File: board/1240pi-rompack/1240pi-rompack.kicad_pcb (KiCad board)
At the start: 4 copper layers, 73.7 x 50.8 mm, 5 parts, among them J1 HDMI_A, J2 HDMI_A, P1 CardEdge_ROMPACK

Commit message: Add more stuff to rompack board.
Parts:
- added R1: 470R, Resistor_SMD:R_0603_1608Metric, F.Cu at (144.8, 81.3)
- added R2: 470R, Resistor_SMD:R_0603_1608Metric, F.Cu at (148.8, 81.3)
- added REF**: QFN-48-1EP_7x7mm_P0.5mm_EP5.15x5.15mm, Package_DFN_QFN:QFN-48-1EP_7x7mm_P0.5mm_EP5.15x5.15mm, F.Cu at (147.3, 94.0)
- added REF**: VQFP-100_14x14mm_P0.5mm, Package_QFP:VQFP-100_14x14mm_P0.5mm, F.Cu at (168.9, 83.8)
- moved J1 9.17 mm to (177.8, 104.9)
- moved J2 9.17 mm to (158.8, 104.9)
- moved J3 5.09 mm to (132.4, 102.2)
- moved A1 1.76 mm to (187.0, 67.0)
- renumbered J** to J3
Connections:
- A1 pad 10: unconnected-(A1-Pad10) -> Net-(A1-Pad10)
- A1 pad 11: unconnected-(A1-Pad11) -> Net-(A1-Pad11)
- A1 pad 12: unconnected-(A1-Pad12) -> Net-(A1-Pad12)
- A1 pad 143: unconnected-(A1-Pad143) -> /HDMI/HDMI_OUT_HPD
- A1 pad 145: unconnected-(A1-Pad145) -> /HDMI/HDMI_OUT_SDA
- A1 pad 146: unconnected-(A1-Pad146) -> /HDMI/HDMI_OUT_D2_P
- A1 pad 147: unconnected-(A1-Pad147) -> /HDMI/HDMI_OUT_SCL
- A1 pad 148: unconnected-(A1-Pad148) -> /HDMI/HDMI_OUT_D2_N
- A1 pad 149: unconnected-(A1-Pad149) -> /HDMI/HDMI_OUT_CEC
- A1 pad 152: unconnected-(A1-Pad152) -> /HDMI/HDMI_OUT_D1_P
- A1 pad 154: unconnected-(A1-Pad154) -> /HDMI/HDMI_OUT_D1_N
- A1 pad 158: unconnected-(A1-Pad158) -> /HDMI/HDMI_OUT_D0_P
- A1 pad 160: unconnected-(A1-Pad160) -> /HDMI/HDMI_OUT_D0_N
- A1 pad 164: unconnected-(A1-Pad164) -> /HDMI/HDMI_OUT_CK_P
- A1 pad 166: unconnected-(A1-Pad166) -> /HDMI/HDMI_OUT_CK_N
- A1 pad 17: unconnected-(A1-Pad17) -> /CM4 Direct IO/ETH_LED_Y
- A1 pad 19: unconnected-(A1-Pad19) -> /CM4 Direct IO/ETH_LED_G
- A1 pad 3: unconnected-(A1-Pad3) -> Net-(A1-Pad3)
- A1 pad 4: unconnected-(A1-Pad4) -> Net-(A1-Pad4)
- A1 pad 5: unconnected-(A1-Pad5) -> Net-(A1-Pad5)
- A1 pad 6: unconnected-(A1-Pad6) -> Net-(A1-Pad6)
- A1 pad 9: unconnected-(A1-Pad9) -> Net-(A1-Pad9)
- J1 pad 1: unconnected-(J1-Pad1) -> /HDMI/HDMI_IN_D2_P
- J1 pad 10: unconnected-(J1-Pad10) -> /HDMI/HDMI_IN_CK_P
- J1 pad 12: unconnected-(J1-Pad12) -> /HDMI/HDMI_IN_CK_N
- J1 pad 13: unconnected-(J1-Pad13) -> /HDMI/HDMI_IN_CEC
- J1 pad 15: unconnected-(J1-Pad15) -> /HDMI/HDMI_IN_SCL
- J1 pad 16: unconnected-(J1-Pad16) -> /HDMI/HDMI_IN_SDA
- J1 pad 19: unconnected-(J1-Pad19) -> /HDMI/HDMI_IN_HPD
- J1 pad 3: unconnected-(J1-Pad3) -> /HDMI/HDMI_IN_D2_N
- J1 pad 4: unconnected-(J1-Pad4) -> /HDMI/HDMI_IN_D1_P
- J1 pad 6: unconnected-(J1-Pad6) -> /HDMI/HDMI_IN_D1_N
- J1 pad 7: unconnected-(J1-Pad7) -> /HDMI/HDMI_IN_D0_P
- J1 pad 9: unconnected-(J1-Pad9) -> /HDMI/HDMI_IN_D0_N
- J2 pad 1: unconnected-(J2-Pad1) -> /HDMI/HDMI_OUT_D2_P
- J2 pad 10: unconnected-(J2-Pad10) -> /HDMI/HDMI_OUT_CK_P
- J2 pad 12: unconnected-(J2-Pad12) -> /HDMI/HDMI_OUT_CK_N
- J2 pad 13: unconnected-(J2-Pad13) -> /HDMI/HDMI_OUT_CEC
- J2 pad 15: unconnected-(J2-Pad15) -> /HDMI/HDMI_OUT_SCL
- J2 pad 16: unconnected-(J2-Pad16) -> /HDMI/HDMI_OUT_SDA
- J2 pad 18: unconnected-(J2-Pad18) -> /HDMI/HDMI_OUT_+5V
- J2 pad 19: unconnected-(J2-Pad19) -> /HDMI/HDMI_OUT_HPD
- J2 pad 3: unconnected-(J2-Pad3) -> /HDMI/HDMI_OUT_D2_N
- J2 pad 4: unconnected-(J2-Pad4) -> /HDMI/HDMI_OUT_D1_P
- J2 pad 6: unconnected-(J2-Pad6) -> /HDMI/HDMI_OUT_D1_N
- J2 pad 7: unconnected-(J2-Pad7) -> /HDMI/HDMI_OUT_D0_P
- J2 pad 9: unconnected-(J2-Pad9) -> /HDMI/HDMI_OUT_D0_N
- J3 pad 1: (no net) -> Net-(A1-Pad12)
- J3 pad 10: (no net) -> Net-(A1-Pad5)
- J3 pad 2: (no net) -> Net-(A1-Pad10)
- J3 pad 3: (no net) -> Net-(A1-Pad4)
- J3 pad 4: (no net) -> Net-(A1-Pad6)
- J3 pad 5: (no net) -> unconnected-(J3-Pad5)
- J3 pad 6: (no net) -> unconnected-(J3-Pad5)
- J3 pad 7: (no net) -> Net-(A1-Pad11)
- J3 pad 8: (no net) -> Net-(A1-Pad9)
- J3 pad 9: (no net) -> Net-(A1-Pad3)
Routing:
- added copper zone on In1.Cu, net GND
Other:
- board size 73.7 x 50.8 mm -> 76.2 x 50.8 mm
- board text added: "Case opening clearance: top 600 mil, bottom 200 mil"

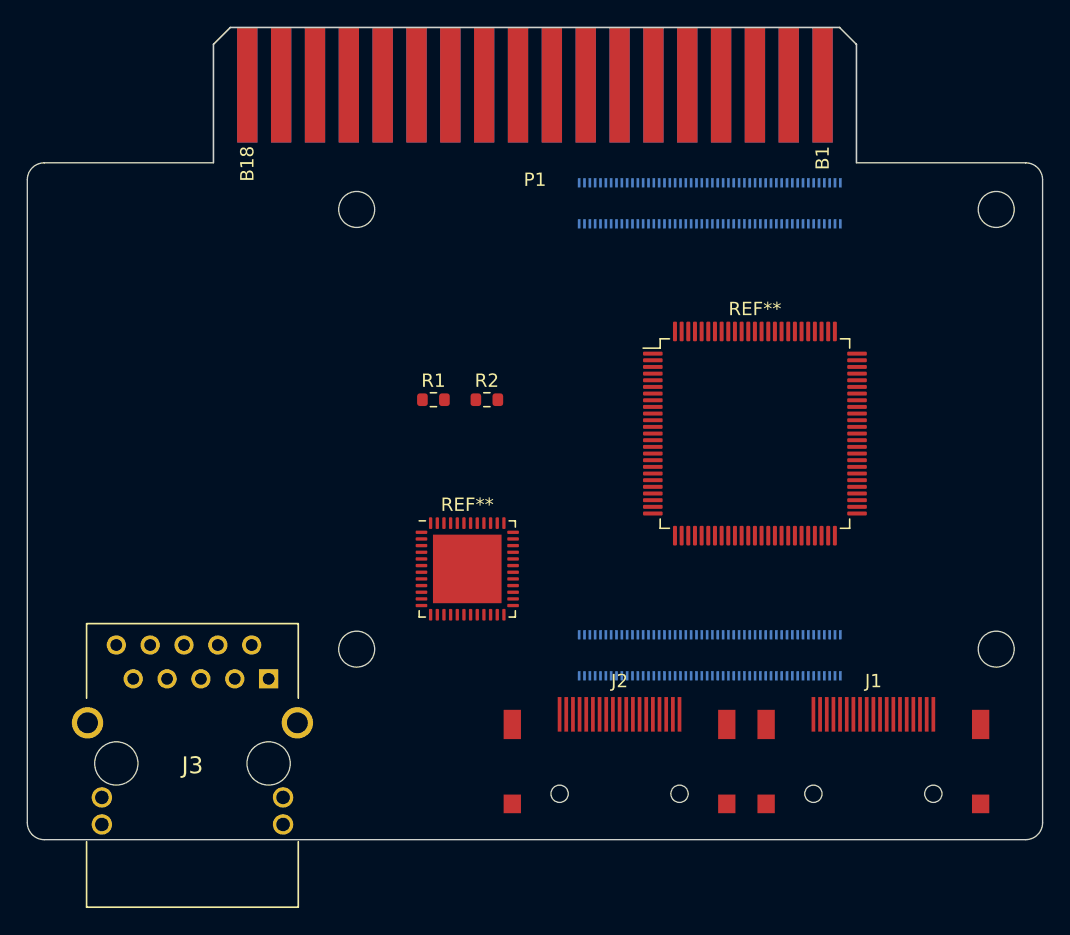
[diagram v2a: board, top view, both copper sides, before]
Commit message: Add buffers to card-edge connector.
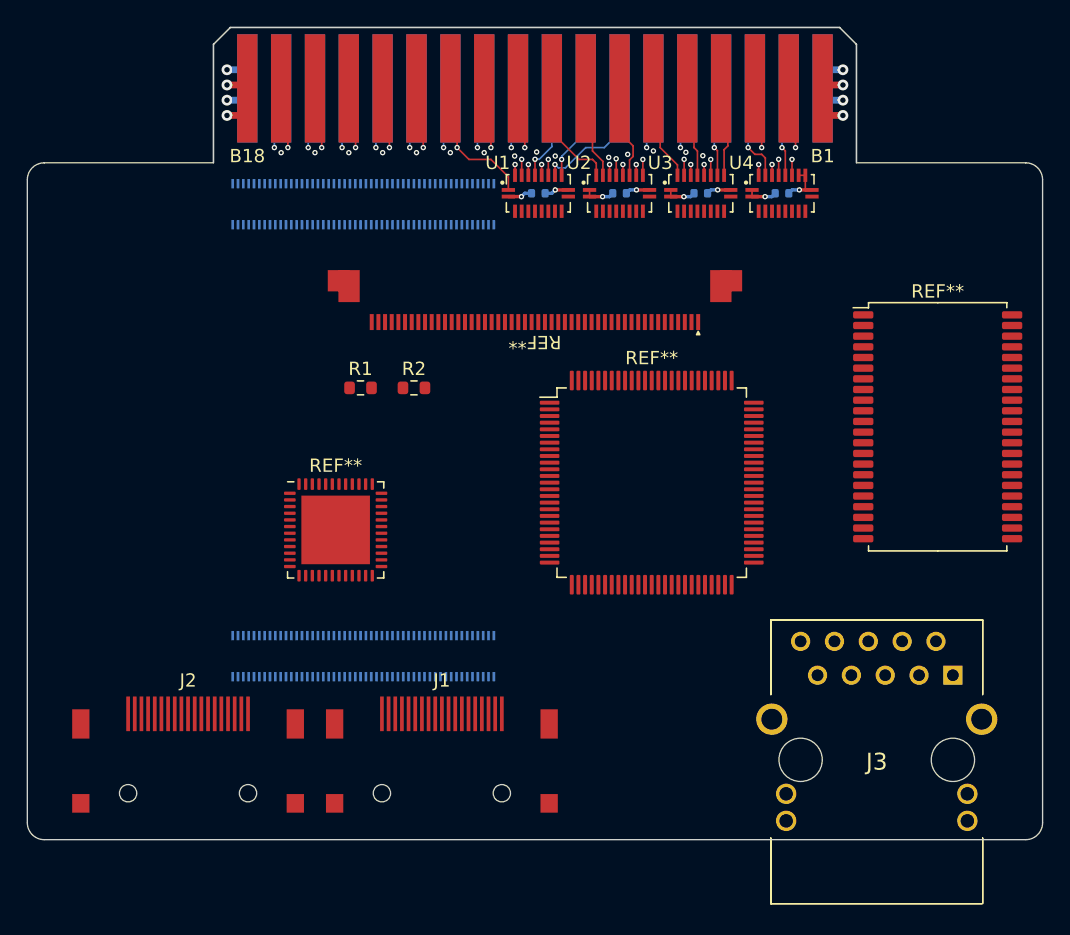
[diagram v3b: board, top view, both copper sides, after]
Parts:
- added C1: 100n, Resistor_SMD:R_0402_1005Metric, B.Cu at (152.7, 65.8)
- added C2: 100n, Resistor_SMD:R_0402_1005Metric, B.Cu at (158.8, 65.8)
- added C3: 100n, Resistor_SMD:R_0402_1005Metric, B.Cu at (164.8, 65.8)
- added C4: 100n, Resistor_SMD:R_0402_1005Metric, B.Cu at (170.9, 65.8)
- added REF**: Amphenol_62684-50210, 0Local:Amphenol_62684-50210, F.Cu at (152.4, 73.2)
- added REF**: SRAM, Package_SO:TSOP-II-44_10.16x18.41mm_P0.8mm, F.Cu at (182.6, 83.3)
- added U1: 74LVC245A, 0Local:Nexperia_SOT764-1, F.Cu at (152.7, 65.8)
- added U2: 74LVC245A, 0Local:Nexperia_SOT764-1, F.Cu at (158.8, 65.8)
- added U3: 74LVC245A, 0Local:Nexperia_SOT764-1, F.Cu at (164.8, 65.8)
- added U4: 74LVC245A, 0Local:Nexperia_SOT764-1, F.Cu at (170.9, 65.8)
- moved A1 76.5 mm to (118.0, 100.1), turned to 90 degrees
- moved J3 51.4 mm to (183.8, 102.0)
- moved J1 32.4 mm to (145.4, 104.9)
- moved J2 32.4 mm to (126.4, 104.9)
- moved REF** 10.3 mm to (137.4, 91.1)
- moved REF** 8.58 mm to (161.2, 87.5)
- moved R1 5.54 mm to (139.3, 80.4)
- moved R2 5.54 mm to (143.3, 80.4)
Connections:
- P1 pad A10: /C_~{CS0} -> /Control Proc Interface/C_~{CS0}
- P1 pad A11: /C_~{CS3} -> /Control Proc Interface/C_~{CS3}
- P1 pad A12: /C_A10 -> /Control Proc Interface/C_A10
- P1 pad A13: /C_~{OE} -> /Control Proc Interface/C_~{OE}
- P1 pad A14: /C_A11 -> /Control Proc Interface/C_A11
- P1 pad A15: /C_D0 -> /Control Proc Interface/C_D0
- P1 pad A16: /C_D1 -> /Control Proc Interface/C_D1
- P1 pad A17: /C_~{CS1} -> /Control Proc Interface/C_~{CS1}
- P1 pad A2: /C_A13 -> /Control Proc Interface/C_A13
- P1 pad A3: /C_A14 -> /Control Proc Interface/C_A14
- P1 pad A4: /C_A15 -> /Control Proc Interface/C_A15
- P1 pad A5: /C_D3 -> /Control Proc Interface/C_D3
- P1 pad A6: /C_D4 -> /Control Proc Interface/C_D4
- P1 pad A7: /C_D5 -> /Control Proc Interface/C_D5
- P1 pad A8: /C_D6 -> /Control Proc Interface/C_D6
- P1 pad A9: /C_D7 -> /Control Proc Interface/C_D7
- P1 pad B10: /C_A8 -> /Control Proc Interface/C_A8
- P1 pad B11: /C_A9 -> /Control Proc Interface/C_A9
- P1 pad B12: /C_~{WE} -> /Control Proc Interface/C_~{WE}
- P1 pad B13: /C_D2 -> /Control Proc Interface/C_D2
- P1 pad B14: /C_A12 -> /Control Proc Interface/C_A12
- P1 pad B15: /C_A0 -> /Control Proc Interface/C_A0
- P1 pad B16: /C_A1 -> /Control Proc Interface/C_A1
- P1 pad B17: /C_~{CS2} -> /Control Proc Interface/C_~{CS2}
- P1 pad B2: /C_SEL1 -> GND
- P1 pad B3: /C_SEL0 -> GND
- P1 pad B4: /C_A2 -> /Control Proc Interface/C_A2
- P1 pad B5: /C_A3 -> /Control Proc Interface/C_A3
- P1 pad B6: /C_A4 -> /Control Proc Interface/C_A4
- P1 pad B7: /C_A5 -> /Control Proc Interface/C_A5
- P1 pad B8: /C_A6 -> /Control Proc Interface/C_A6
- P1 pad B9: /C_A7 -> /Control Proc Interface/C_A7
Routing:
- net /Control Proc Interface/C_~{CS1}: track 0.00 -> 52.4 mm, vias 0 -> 2
- net /Control Proc Interface/C_~{CS2}: track 0.00 -> 49.5 mm, vias 0 -> 2
- net /Control Proc Interface/C_A1: track 0.00 -> 45.7 mm, vias 0 -> 2
- net /Control Proc Interface/C_A0: track 0.00 -> 41.6 mm, vias 0 -> 2
- net /Control Proc Interface/C_A11: track 0.00 -> 36.7 mm, vias 0 -> 2
- net /Control Proc Interface/C_A12: track 0.00 -> 34.3 mm, vias 0 -> 2
- net /Control Proc Interface/C_~{OE}: track 0.00 -> 31.3 mm, vias 0 -> 2
- net GND: track 0.00 -> 29.5 mm, vias 0 -> 25
- net /Control Proc Interface/C_~{WE}: track 0.00 -> 28.8 mm, vias 0 -> 2
- net /Control Proc Interface/C_A10: track 0.00 -> 27.3 mm, vias 0 -> 2
- net /Control Proc Interface/C_D1: track 0.00 -> 25.7 mm, vias 0 -> 2
- net /Control Proc Interface/C_D0: track 0.00 -> 21.6 mm, vias 0 -> 2
- net /Control Proc Interface/C_~{CS3}: track 0.00 -> 20.3 mm, vias 0 -> 2
- net /Control Proc Interface/C_D3: track 0.00 -> 18.1 mm, vias 0 -> 2
- net /Control Proc Interface/C_A9: track 0.00 -> 17.8 mm, vias 0 -> 2
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- added copper zone on In3.Cu, net +3V3
- added copper zone on In2.Cu, net +5V
- added copper zone on In4.Cu, net GND
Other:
- copper layers 4 -> 6
- rule pad_to_mask_clearance: 0 -> 0.0762

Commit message: Split connectors out of CM4 footprint.
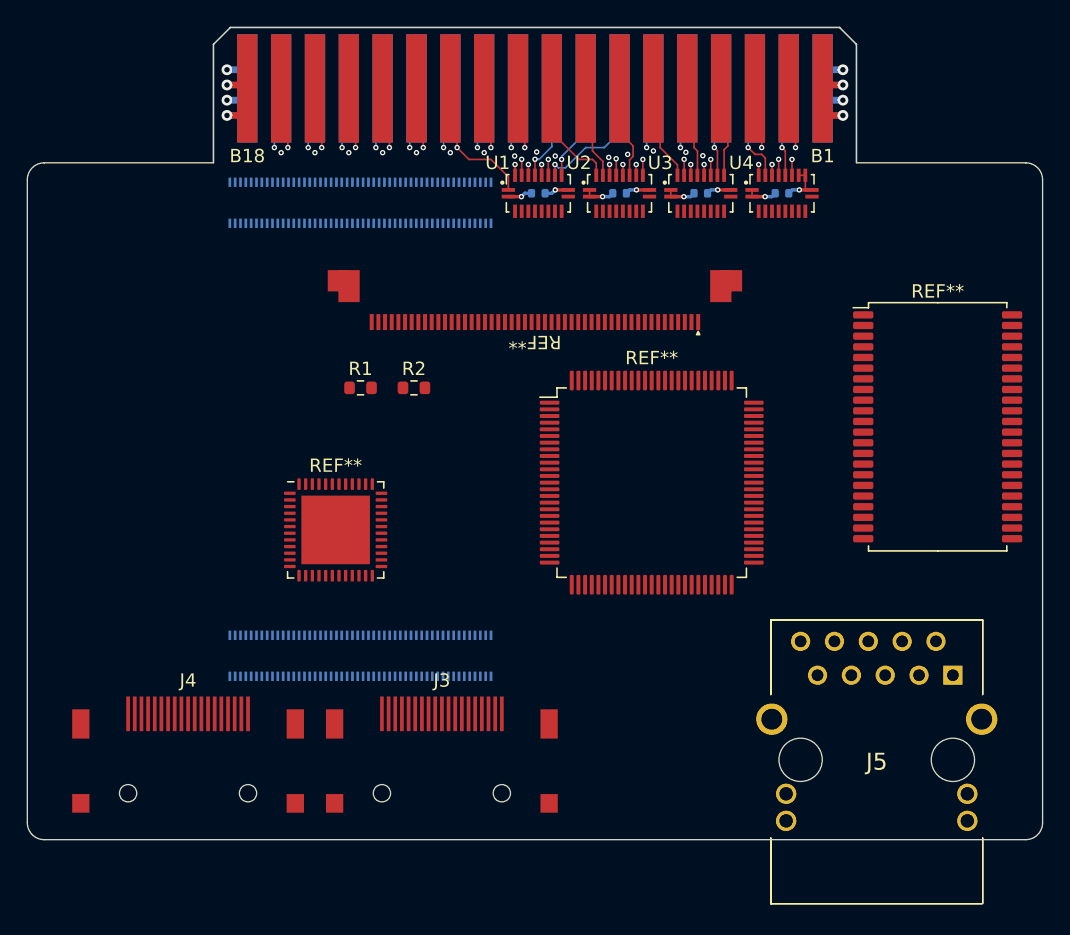
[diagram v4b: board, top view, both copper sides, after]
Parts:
- removed A1: RaspberryPi_CM4, 0Local:RaspberryPi_CM4
- added J1: RaspberryPi_CM4_A, 0Local:Hirose_DF40C-100DS-0.4V, B.Cu at (139.3, 100.5)
- added J2: RaspberryPi_CM4_B, 0Local:Hirose_DF40C-100DS-0.4V, B.Cu at (139.3, 66.5)
- added REF**: RaspberryPi_CM4, 0Local:RaspberryPi_CM4, B.Cu at (165.8, 100.0)
- renumbered J1 to J3, J2 to J4, J3 to J5

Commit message: Route HDMI output port.
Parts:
- removed the REF** at (137.4, 91.1)
- added MH1: MountingHole_2.7mm_M2.5, MountingHole:MountingHole_2.7mm_M2.5, F.Cu at (117.8, 100.0)
- added MH1: MountingHole_2.7mm_M2.5, MountingHole:MountingHole_2.7mm_M2.5, F.Cu at (165.8, 100.0)
- added MH1: MountingHole_2.7mm_M2.5, MountingHole:MountingHole_2.7mm_M2.5, F.Cu at (117.8, 67.0)
- moved R2 36.7 mm to (164.6, 110.2)
- moved R1 36.7 mm to (160.6, 110.2)
- moved REF** 26.1 mm to (157.5, 90.2), turned to 90 degrees
- moved REF** 18.1 mm to (179.1, 85.1)
- moved J5 8.85 mm to (178.1, 108.7)
- moved J3 1.40 mm to (126.4, 106.3)
- moved J4 1.40 mm to (145.4, 106.3)
- renumbered J4 to J3, J3 to J4
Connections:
- J1 pad 78: unconnected-(J1-Pad78) -> /+3V3_PI
- J1 pad 84: /PI_GPIO_VREF -> /+3V3_PI
- J1 pad 86: /PI_GPIO_VREF -> /+3V3_PI
- J2 pad 1: (no net) -> unconnected-(J2-Pad1)
- J2 pad 10: (no net) -> unconnected-(J2-Pad10)
- J2 pad 100: (no net) -> /HDMI/HDMI_OUT_SCL
- J2 pad 11: (no net) -> unconnected-(J2-Pad11)
- J2 pad 12: (no net) -> unconnected-(J2-Pad12)
- J2 pad 13: (no net) -> GND
- J2 pad 14: (no net) -> GND
- J2 pad 15: (no net) -> unconnected-(J2-Pad15)
- J2 pad 16: (no net) -> unconnected-(J2-Pad16)
- J2 pad 17: (no net) -> unconnected-(J2-Pad17)
- J2 pad 18: (no net) -> unconnected-(J2-Pad18)
- J2 pad 19: (no net) -> GND
- J2 pad 2: (no net) -> unconnected-(J2-Pad2)
- J2 pad 20: (no net) -> GND
- J2 pad 21: (no net) -> unconnected-(J2-Pad21)
- J2 pad 22: (no net) -> unconnected-(J2-Pad22)
- J2 pad 23: (no net) -> unconnected-(J2-Pad23)
- J2 pad 24: (no net) -> unconnected-(J2-Pad24)
- J2 pad 25: (no net) -> GND
- J2 pad 26: (no net) -> GND
- J2 pad 27: (no net) -> unconnected-(J2-Pad27)
- J2 pad 28: (no net) -> unconnected-(J2-Pad28)
- J2 pad 29: (no net) -> unconnected-(J2-Pad29)
- J2 pad 3: (no net) -> unconnected-(J2-Pad3)
- J2 pad 30: (no net) -> unconnected-(J2-Pad30)
- J2 pad 31: (no net) -> GND
- J2 pad 32: (no net) -> GND
- J2 pad 33: (no net) -> unconnected-(J2-Pad33)
- J2 pad 34: (no net) -> unconnected-(J2-Pad34)
- J2 pad 35: (no net) -> unconnected-(J2-Pad35)
- J2 pad 36: (no net) -> unconnected-(J2-Pad36)
- J2 pad 37: (no net) -> GND
- J2 pad 38: (no net) -> GND
- J2 pad 39: (no net) -> unconnected-(J2-Pad39)
- J2 pad 4: (no net) -> unconnected-(J2-Pad4)
- J2 pad 40: (no net) -> unconnected-(J2-Pad40)
- J2 pad 41: (no net) -> unconnected-(J2-Pad41)
- J2 pad 42: (no net) -> unconnected-(J2-Pad42)
- J2 pad 43: (no net) -> unconnected-(J2-Pad43)
- J2 pad 44: (no net) -> GND
- J2 pad 45: (no net) -> unconnected-(J2-Pad45)
- J2 pad 46: (no net) -> unconnected-(J2-Pad46)
- J2 pad 47: (no net) -> unconnected-(J2-Pad47)
- J2 pad 48: (no net) -> unconnected-(J2-Pad48)
- J2 pad 49: (no net) -> unconnected-(J2-Pad49)
- J2 pad 5: (no net) -> unconnected-(J2-Pad5)
- J2 pad 50: (no net) -> GND
- J2 pad 51: (no net) -> /HDMI/HDMI_OUT_CEC
- J2 pad 52: (no net) -> unconnected-(J2-Pad52)
- J2 pad 53: (no net) -> /HDMI/HDMI_OUT_HPD
- J2 pad 54: (no net) -> unconnected-(J2-Pad54)
- J2 pad 55: (no net) -> GND
- J2 pad 56: (no net) -> GND
- J2 pad 57: (no net) -> unconnected-(J2-Pad57)
- J2 pad 58: (no net) -> unconnected-(J2-Pad58)
- J2 pad 59: (no net) -> unconnected-(J2-Pad59)
- J2 pad 6: (no net) -> unconnected-(J2-Pad6)
- J2 pad 60: (no net) -> unconnected-(J2-Pad60)
- J2 pad 61: (no net) -> GND
- J2 pad 62: (no net) -> GND
- J2 pad 63: (no net) -> unconnected-(J2-Pad63)
- J2 pad 64: (no net) -> unconnected-(J2-Pad64)
- J2 pad 65: (no net) -> unconnected-(J2-Pad65)
- J2 pad 66: (no net) -> unconnected-(J2-Pad66)
- J2 pad 67: (no net) -> GND
- J2 pad 68: (no net) -> GND
- J2 pad 69: (no net) -> unconnected-(J2-Pad69)
- J2 pad 7: (no net) -> GND
- J2 pad 70: (no net) -> /HDMI/HDMI_OUT_D2_P
- J2 pad 71: (no net) -> unconnected-(J2-Pad71)
- J2 pad 72: (no net) -> /HDMI/HDMI_OUT_D2_N
- J2 pad 73: (no net) -> GND
- J2 pad 74: (no net) -> GND
- J2 pad 75: (no net) -> unconnected-(J2-Pad75)
- J2 pad 76: (no net) -> /HDMI/HDMI_OUT_D1_P
- J2 pad 77: (no net) -> unconnected-(J2-Pad77)
- J2 pad 78: (no net) -> /HDMI/HDMI_OUT_D1_N
- J2 pad 79: (no net) -> GND
- J2 pad 8: (no net) -> GND
- J2 pad 80: (no net) -> GND
- J2 pad 81: (no net) -> unconnected-(J2-Pad81)
- J2 pad 82: (no net) -> /HDMI/HDMI_OUT_D0_P
- J2 pad 83: (no net) -> unconnected-(J2-Pad83)
- J2 pad 84: (no net) -> /HDMI/HDMI_OUT_D0_N
- J2 pad 85: (no net) -> GND
- J2 pad 86: (no net) -> GND
- J2 pad 87: (no net) -> unconnected-(J2-Pad87)
- J2 pad 88: (no net) -> /HDMI/HDMI_OUT_CK_P
- J2 pad 89: (no net) -> unconnected-(J2-Pad89)
- J2 pad 9: (no net) -> unconnected-(J2-Pad9)
- J2 pad 90: (no net) -> /HDMI/HDMI_OUT_CK_N
- J2 pad 91: (no net) -> GND
- J2 pad 92: (no net) -> GND
- J2 pad 93: (no net) -> unconnected-(J2-Pad93)
- J2 pad 94: (no net) -> unconnected-(J2-Pad94)
- J2 pad 95: (no net) -> unconnected-(J2-Pad95)
- J2 pad 96: (no net) -> unconnected-(J2-Pad96)
- J2 pad 97: (no net) -> GND
- J2 pad 98: (no net) -> GND
- J2 pad 99: (no net) -> /HDMI/HDMI_OUT_SDA
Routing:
- net GND: track 29.5 -> 80.8 mm, vias 25 -> 95
- net /HDMI/HDMI_OUT_HPD: track 0.00 -> 51.2 mm, vias 0 -> 2
- net /HDMI/HDMI_OUT_CEC: track 0.00 -> 49.0 mm, vias 0 -> 2
- net /HDMI/HDMI_OUT_D0_N: track 0.00 -> 46.3 mm, vias 0 -> 2
- net /HDMI/HDMI_OUT_D0_P: track 0.00 -> 46.3 mm, vias 0 -> 2
- net /HDMI/HDMI_OUT_D2_N: track 0.00 -> 46.1 mm, vias 0 -> 2
- net /HDMI/HDMI_OUT_D2_P: track 0.00 -> 46.1 mm, vias 0 -> 2
- net /HDMI/HDMI_OUT_SCL: track 0.00 -> 44.4 mm, vias 0 -> 2
- net /HDMI/HDMI_OUT_CK_N: track 0.00 -> 43.9 mm, vias 0 -> 2
- net /HDMI/HDMI_OUT_CK_P: track 0.00 -> 43.9 mm, vias 0 -> 2
- net /HDMI/HDMI_OUT_D1_N: track 0.00 -> 43.7 mm, vias 0 -> 2
- net /HDMI/HDMI_OUT_D1_P: track 0.00 -> 43.7 mm, vias 0 -> 2
- net /HDMI/HDMI_OUT_SDA: track 0.00 -> 40.8 mm, vias 0 -> 2
- net +5V: track 10.7 -> 0.00 mm, vias 4 -> 12
- net /HDMI/HDMI_OUT_+5V: track 0.00 -> 3.12 mm
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- added copper zone on B.Cu, net +5V
- added copper zone on F.Cu, net +5V
- added copper zone on B.Cu, net /+3V3_PI
- added copper zone on B.Cu, net GND
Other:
- board text added: "100 ohm diff pair: inner 10.5 mil trace / 5 mil separation outer 5 mil trace / 5 mil separation"
